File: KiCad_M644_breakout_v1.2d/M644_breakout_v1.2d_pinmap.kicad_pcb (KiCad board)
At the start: 2 copper layers, 54.6 x 45 mm, 62 parts, among them IC1 ATMEGA16/32/644/1284, IC2 78TV, Q1 16Mhz, SW1/PC5 SMD_TACT_4x4, X2 DG300-5.0-02P-12

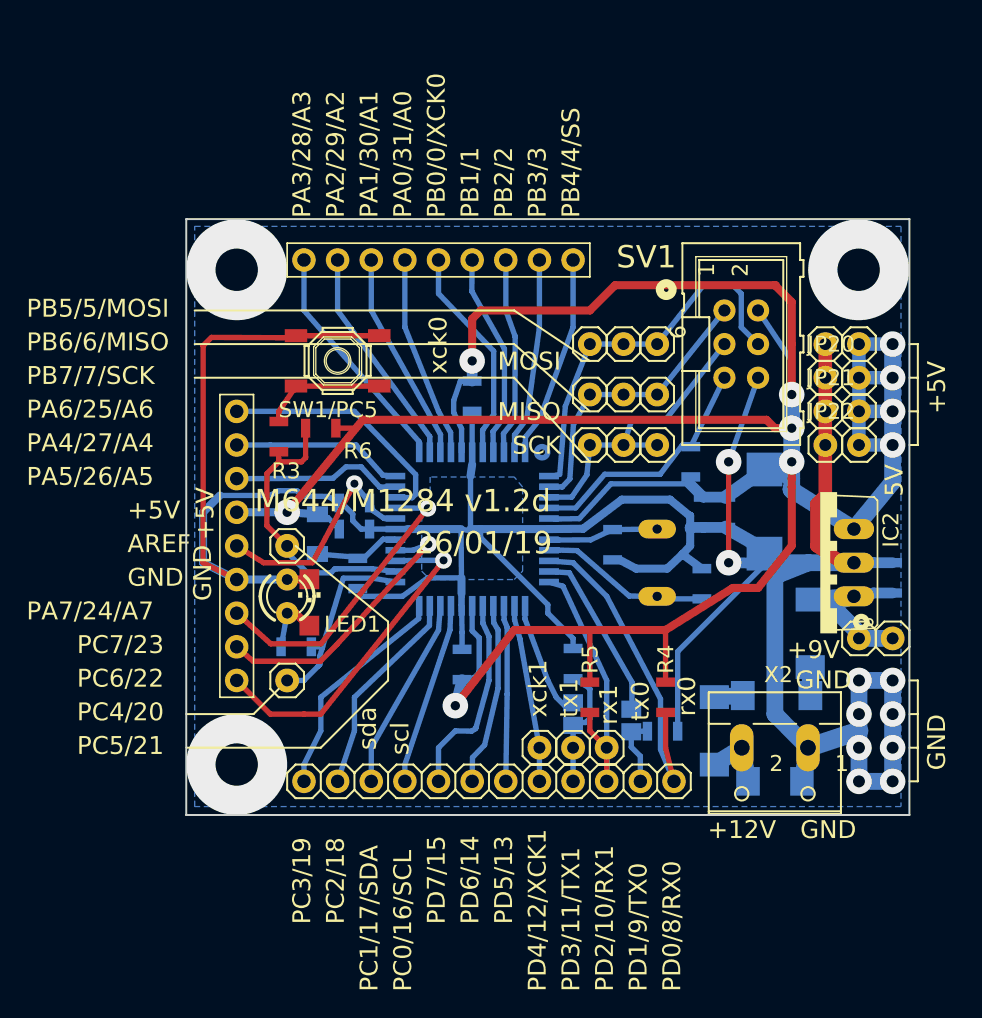
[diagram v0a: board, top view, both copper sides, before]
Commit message: Slightly edited the pics and pcb hardware board
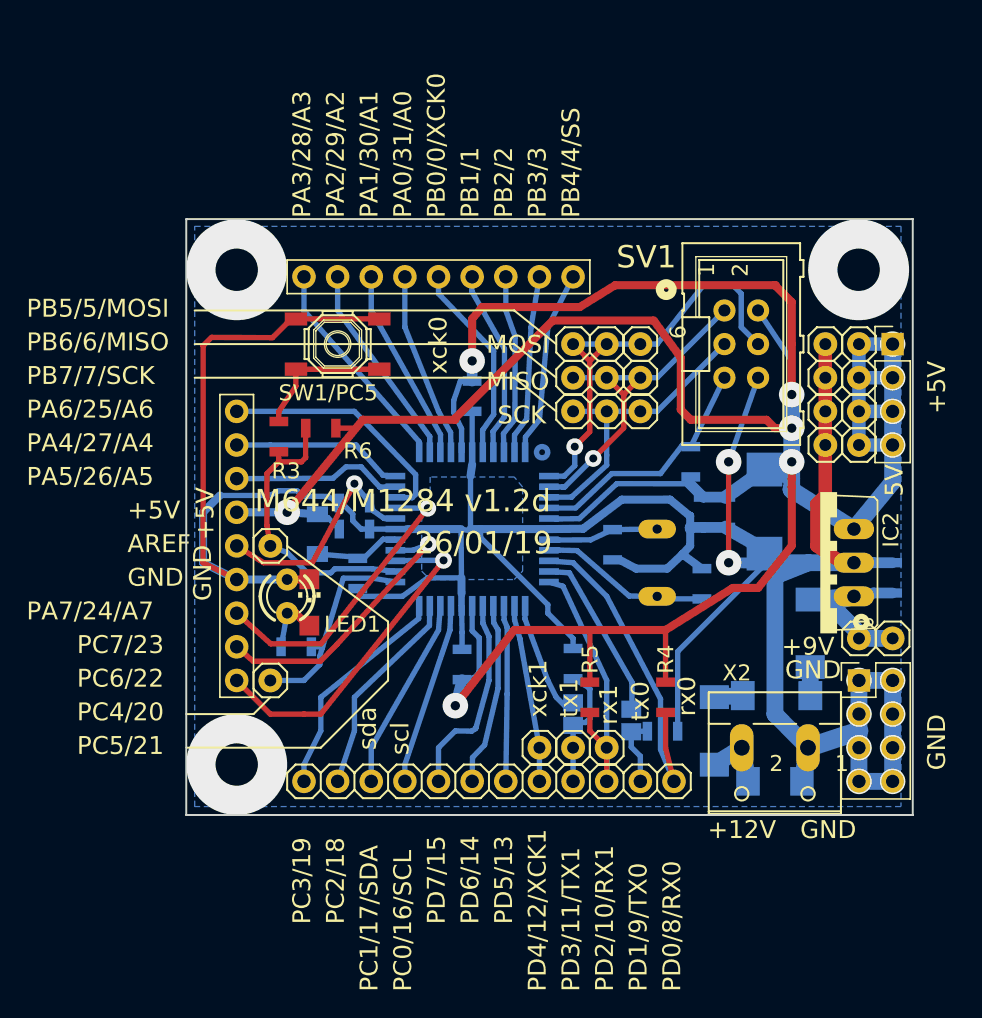
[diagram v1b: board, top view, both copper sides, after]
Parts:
- added REF**: Pin_Header_Straight_2x04_Pitch2.54mm, Pin_Headers:Pin_Header_Straight_2x04_Pitch2.54mm, F.Cu at (172.0, 117.3)
- added REF**: Pin_Header_Straight_1x04_Pitch2.54mm, Pin_Headers:Pin_Header_Straight_1x04_Pitch2.54mm, F.Cu at (174.5, 91.9)
- moved JP11 2.84 mm to (155.5, 97.0)
- moved JP5 2.84 mm to (152.9, 97.0)
- moved JP4 2.84 mm to (150.4, 97.0)
- moved JP12 1.80 mm to (155.5, 94.5)
- moved JP6 1.80 mm to (152.9, 94.5)
- moved JP7 1.80 mm to (150.4, 94.5)
- moved JP1 1.27 mm to (140.2, 86.9)
- moved JP13 1.27 mm to (155.5, 91.9)
- moved JP27 1.27 mm to (127.5, 107.2)
- moved JP28 1.27 mm to (127.5, 117.3)
- moved JP9 1.27 mm to (152.9, 91.9)
- moved SW1/PC5 1.27 mm to (132.6, 91.9)
- moved JP8 1.27 mm to (150.4, 91.9)
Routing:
- net VCC: track 224.0 -> 232.6 mm
- net /MISO: track 21.7 -> 27.2 mm, vias 0 -> 1
- net /MOSI: track 29.2 -> 33.7 mm, vias 0 -> 1
- net /PB3: track 14.9 -> 13.6 mm
- net /PA3: track 17.8 -> 16.5 mm
- net /PC4: track 14.6 -> 15.8 mm
- net Net-(R3-PadP$1): track 9.37 -> 10.6 mm
- net /PA1: track 15.9 -> 14.6 mm
- net /PA0: track 15.3 -> 14.0 mm
- net /PB2: track 15.0 -> 13.7 mm
- net /PA2: track 16.8 -> 15.5 mm
- net /PB0: track 16.5 -> 15.2 mm
- net /PB1: track 15.5 -> 14.2 mm
- net /PB4: track 15.3 -> 14.1 mm
- net GND: track 247.0 -> 247.6 mm
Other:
- board size 54.6 x 45 mm -> 54.9 x 45 mm
